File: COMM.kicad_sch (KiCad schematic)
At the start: 14 parts, among them J1 SMA Conn. (RFPC-SMA29-F), SW1 Inhibit Switch (SS5GLD2), U1 AX.25 Module (DMR818SU), U2 XBee Module (XBP9B-DMSTB002)

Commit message: Finished schematic and fully routed PCB.
Signed-off-by: Logan Tolbert <xem6df@virginia.edu>
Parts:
- removed J1: SMA Conn. (RFPC-SMA29-F), RFPC-SMA29-F:GRADCONN_RFPC-SMA29-F, symbol RFPC-SMA29-F:RFPC-SMA29-F
- removed U1: AX.25 Module (DMR818SU), DMR818S:DMR818SU, symbol DMR818S:DMR818S-U
- added D2: Voltage Converter DMR (1N4002), Diode_THT:D_DO-41_SOD81_P10.16mm_Horizontal, symbol Diode:1N4002
- added J1: SMA Conn. (RFPC-SMA30-F), RFPC-SMA30-F:GRADCONN_RFPC-SMA30-F, symbol RFPC-SMA30-F:RFPC-SMA30-F
- R2: value 10Ω -> 470 Ω
- renumbered D2 to D3, U2 to U1
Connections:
- net PWM0_XB is gone; now on net DIO10/PWM0_XB: U1.6 (DIO10/PWM0)
- net PWM1_XB is gone; now on net DIO11/PWM1_XB: U1.7 (DIO11/PWM1)
- net SLEEP_XB is gone; now on net ON_SLEEP/DIO9_XB: U1.13 (ON_NSLEEP/DIO9)
- net X_RESET is gone; now on net RESET_XB: U1.5 (~{RESET})
- net +3.3V: now also C2.1, C3.1, C4.1, U1.1 (VCC); no longer SW1.2 (B)
- net +5V: now also SW1.2 (B)
- net CS_DMR: now also H2.24; no longer H1.13
- net GND: now also J1.G1, J1.G2, J1.G3, J1.G4
- net HST_RXD_DMR: now also H2.25; no longer H1.19
- net HST_TXD_DMR: now also H2.27; no longer H1.17
- net PTT_DMR: now also H2.22; no longer H1.15
- net T/R_DMR: now also H2.21; no longer H1.11
- net UART_D_RX: no longer U1.3 (DIN/NCONFIG/DIO14)
- net UART_D_TX: no longer U1.2 (DOUT/DIO13)
- net DIO4/SPI_MOSI_XB: now reaches U1.11 (DIO4/SPI_MOSI)
- net DIO4/SPI_MOSI_XB: now also H2.7
- net Associate/DIO5_XB: now reaches D3.2 (A), U1.15 (ASSOCIATE/DIO5)
- net Associate/DIO5_XB: now also H2.16
- net AD3/DIO3/SPI_SSEL_XB: now reaches U1.17 (AD3/DIO3/SPI_NSSEL)
- net AD3/DIO3/SPI_SSEL_XB: now also H2.5
- net AD2/DIO2/SPI_CLK_XB: now reaches U1.18 (AD2/DIO2/SPI_CLK)
- net AD2/DIO2/SPI_CLK_XB: now also H2.6
- net AD1/DIO1/SPI_ATTN_XB: now reaches U1.19 (AD1/DIO1/SPI_NATTN)
- net AD1/DIO1/SPI_ATTN_XB: now also H2.10
- net DIO12/SPI_MISO: now reaches U1.4 (DIO12/SPI_MISO)
- net DIO12/SPI_MISO: now also H2.8
- net DTR/SLEEP_RQ/DIO8: now reaches U1.9 (NDTR/SLEEP_RQ/DIO8)
- net DTR/SLEEP_RQ/DIO8: now also H2.9
- net DIN/CONFIG/DIO14_XB: now reaches H2.1
- net DIN/CONFIG/DIO14_XB: now also U1.3 (DIN/NCONFIG/DIO14)
- net ON_SLEEP/DIO9_XB: now reaches H2.11
- net DIO10/PWM0_XB: now reaches H2.12
- net RESET_XB: now reaches H2.13
- net DIO11/PWM1_XB: now reaches H2.14
- net AD0/DIO0_XB: now reaches H2.15
- net AD0/DIO0_XB: now also U1.20 (AD0/DIO0)
- net NDTR_XB: now reaches H2.17
- net MIC_IN_DMR: now reaches H2.19
- net DOUT/DIO13_XB: now reaches H2.2
- net DOUT/DIO13_XB: now also U1.2 (DOUT/DIO13)
- net LINE_OUT_DMR: now reaches H2.20
- net SPKEN_DMR: now reaches H2.23
- net UART_RX_DMR: now reaches H2.26
- net UART_TX_DMR: now reaches H2.28
- net RTS/DOI6_XB: now reaches H2.3
- net RTS/DOI6_XB: now also U1.16 (NRTS/DIO6)
- net CTS/DIO7_XB: now reaches H2.4
- net CTS/DIO7_XB: now also U1.12 (NCTS/DIO7)
- net CTS_XB: no longer names the net of H1.5
- net CTS_XB: no longer U1.12 (NCTS/DIO7)
- net GPIO_XB: no longer names the net of H1.9
- net GPIO_XB: no longer U1.20 (AD0/DIO0)
- net RTS_XB: no longer names the net of H1.7
- net RTS_XB: no longer U1.16 (NRTS/DIO6)
- new net DMR818S-U 2W RF Module/ANT: J1.1
- new net DMR818S-U 2W RF Module/VCC: D2.1 (K)
- new net Voltage Converter XB/VIN: D2.2 (A), R2.2, SW1.1 (A)
- no-connect marks 0 -> 1
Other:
- sheet Voltage Converter renamed Voltage Converter XB
- added sheet DMR818S-U 2W RF Module (dmrRFMod.kicad_sch)
- moved on the sheet: C1, C2, C3, C4, D1, D3, H1, H2, R1, R2, SW1, U1

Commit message: Added 3D models to all components except DMR module, need to make a 3D model for that one.
Signed-off-by: Logan Tolbert <xem6df@virginia.edu>
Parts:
- R1: footprint Resistor_SMD:R_0805_2012Metric -> R_10kO:RESC1005X40N
- R2: footprint R_10OHM:RESC1005X40 -> R_470O:RESC6332X65N
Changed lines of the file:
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@@
 			)
 		)
-		(property "Footprint" "R_10OHM:RESC1005X40"
+		(property "Footprint" "R_470O:RESC6332X65N"
 			(at 127.254 63.246 90)
 			(effects
@@
 			)
 		)
-		(property "Footprint" "Resistor_SMD:R_0805_2012Metric"
+		(property "Footprint" "R_10kO:RESC1005X40N"
 			(at 115.824 48.006 90)
 			(effects

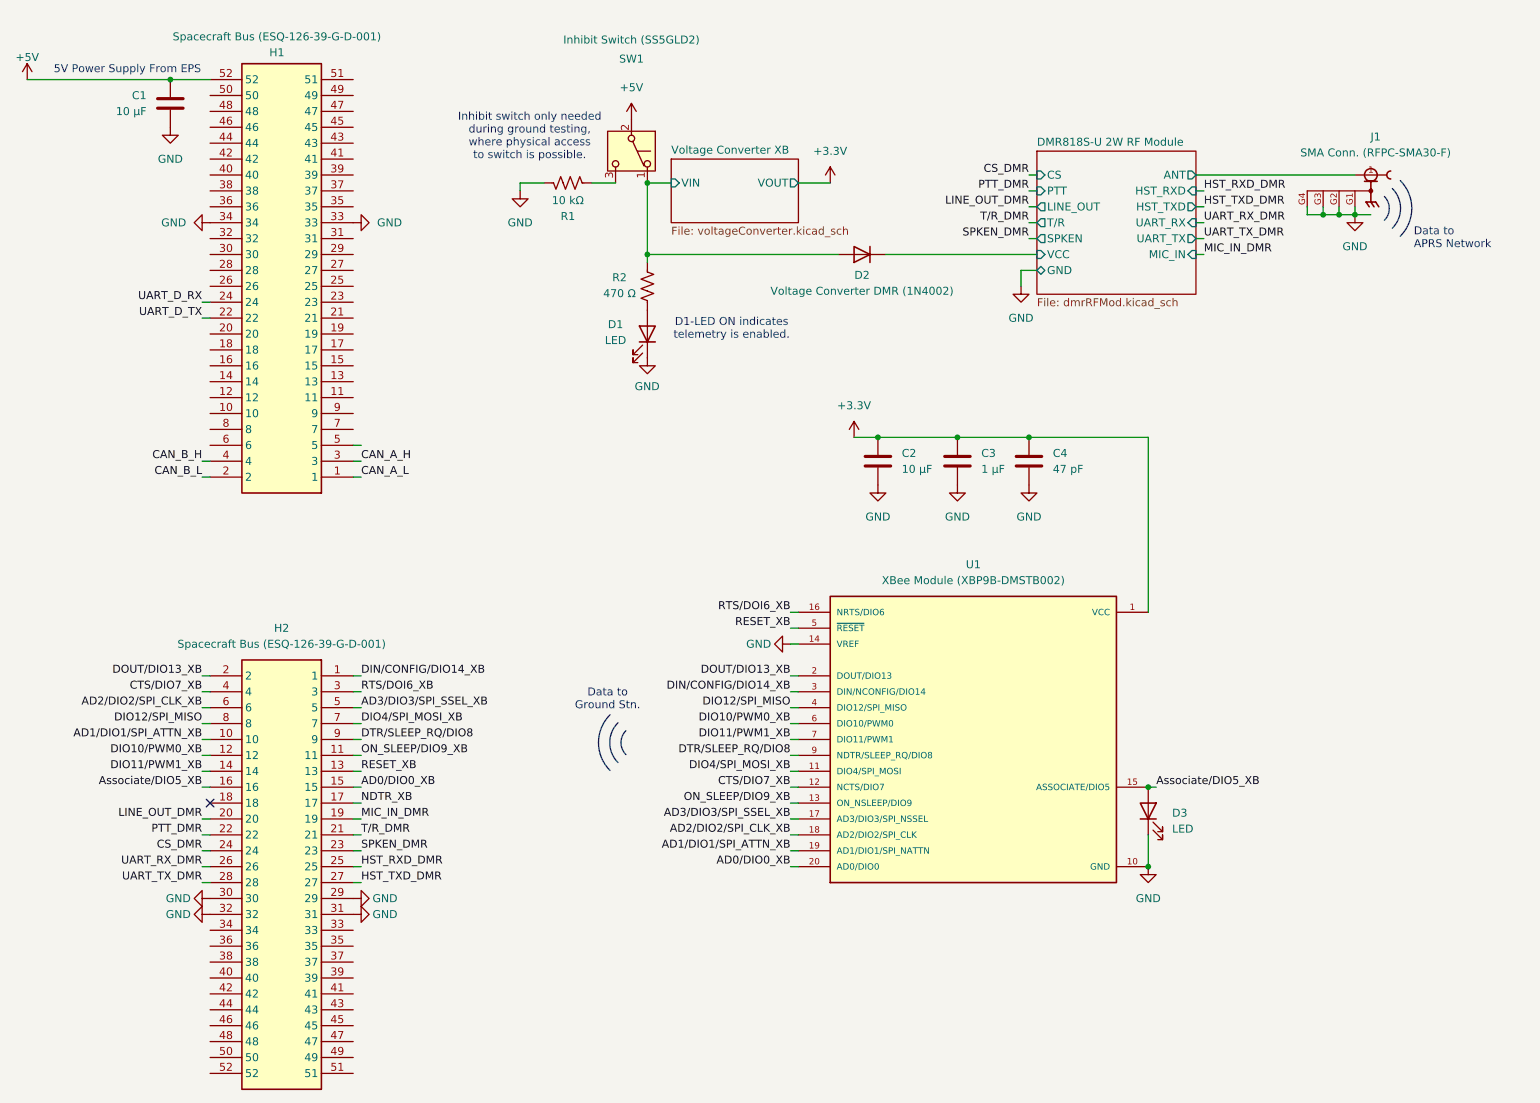
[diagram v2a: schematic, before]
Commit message: removed extraneous connections to the XBee and DMR modules on schematic and PCB.
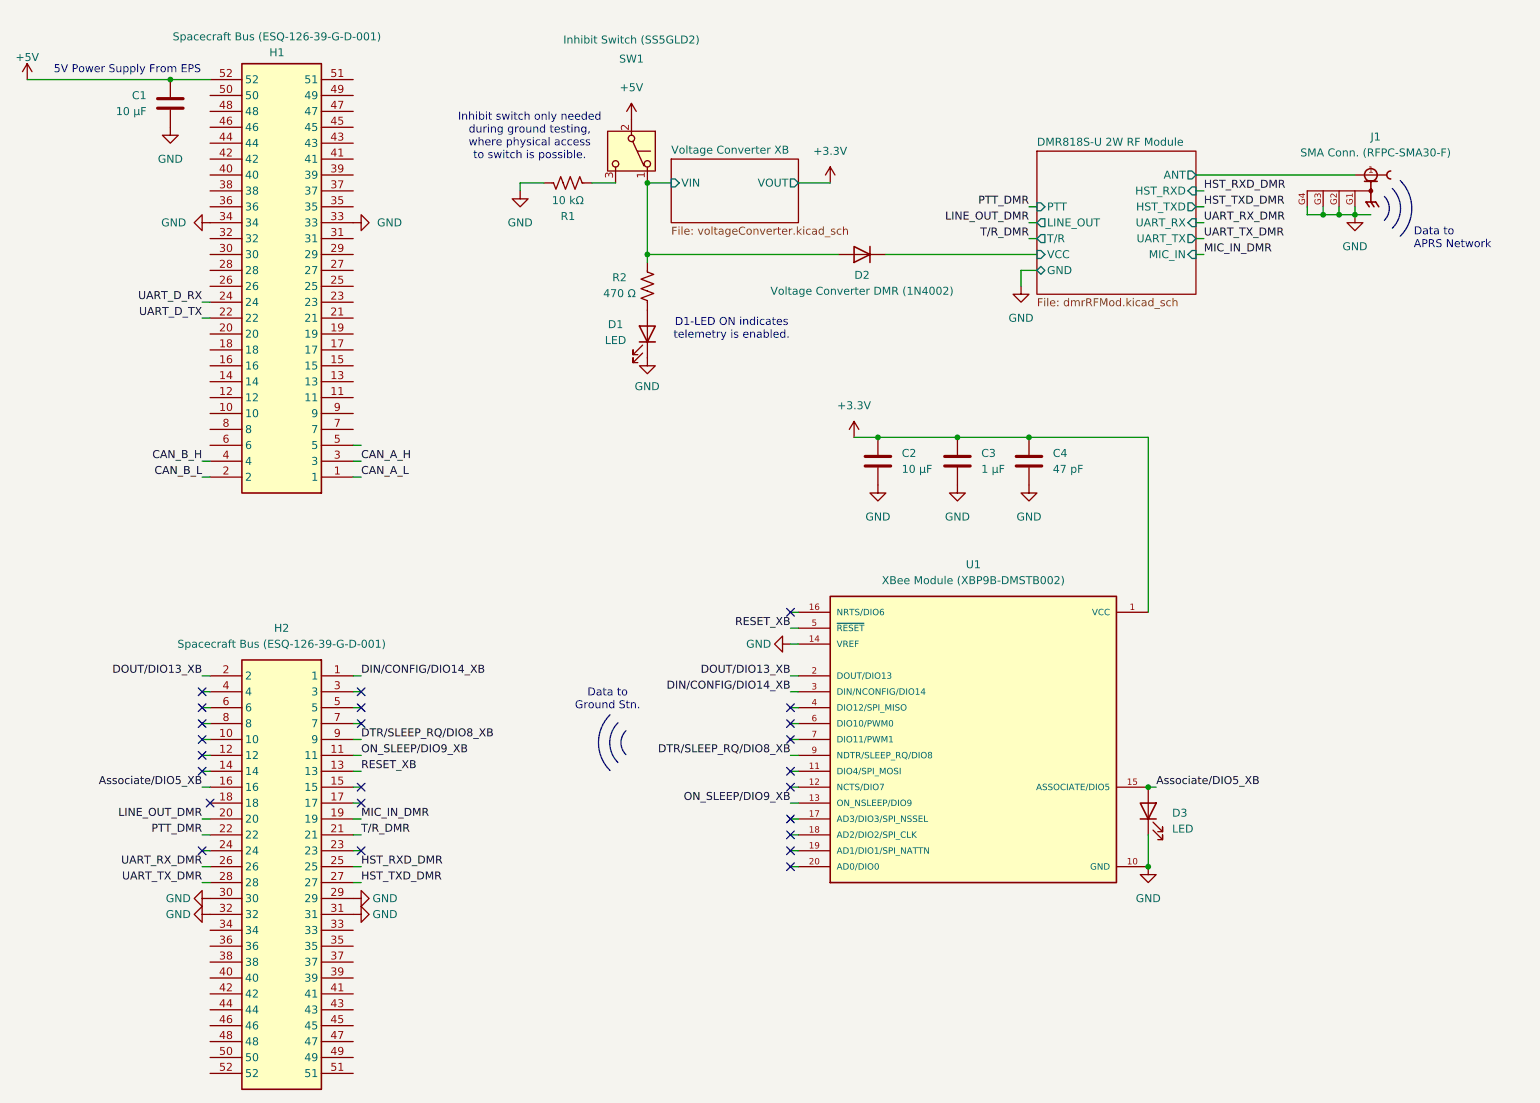
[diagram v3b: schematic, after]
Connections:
- net AD0/DIO0_XB: no longer names the net of U1.20 (AD0/DIO0)
- net AD0/DIO0_XB: no longer H2.15
- net AD1/DIO1/SPI_ATTN_XB: no longer names the net of U1.19 (AD1/DIO1/SPI_NATTN)
- net AD1/DIO1/SPI_ATTN_XB: no longer H2.10
- net AD2/DIO2/SPI_CLK_XB: no longer names the net of U1.18 (AD2/DIO2/SPI_CLK)
- net AD2/DIO2/SPI_CLK_XB: no longer H2.6
- net AD3/DIO3/SPI_SSEL_XB: no longer names the net of U1.17 (AD3/DIO3/SPI_NSSEL)
- net AD3/DIO3/SPI_SSEL_XB: no longer H2.5
- net CS_DMR: no longer names the net of H2.24
- net CTS/DIO7_XB: no longer names the net of U1.12 (NCTS/DIO7)
- net CTS/DIO7_XB: no longer H2.4
- net DIO10/PWM0_XB: no longer names the net of U1.6 (DIO10/PWM0)
- net DIO10/PWM0_XB: no longer H2.12
- net DIO11/PWM1_XB: no longer names the net of U1.7 (DIO11/PWM1)
- net DIO11/PWM1_XB: no longer H2.14
- net DIO12/SPI_MISO: no longer names the net of U1.4 (DIO12/SPI_MISO)
- net DIO12/SPI_MISO: no longer H2.8
- net DIO4/SPI_MOSI_XB: no longer names the net of U1.11 (DIO4/SPI_MOSI)
- net DIO4/SPI_MOSI_XB: no longer H2.7
- net DTR/SLEEP_RQ/DIO8 renamed DTR/SLEEP_RQ/DIO8_XB
- net NDTR_XB: no longer names the net of H2.17
- net RTS/DOI6_XB: no longer names the net of U1.16 (NRTS/DIO6)
- net RTS/DOI6_XB: no longer H2.3
- net SPKEN_DMR: no longer names the net of H2.23
- no-connect marks 1 -> 24
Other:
- sheet DMR818S-U 2W RF Module ports: added none; removed CS, SPKEN

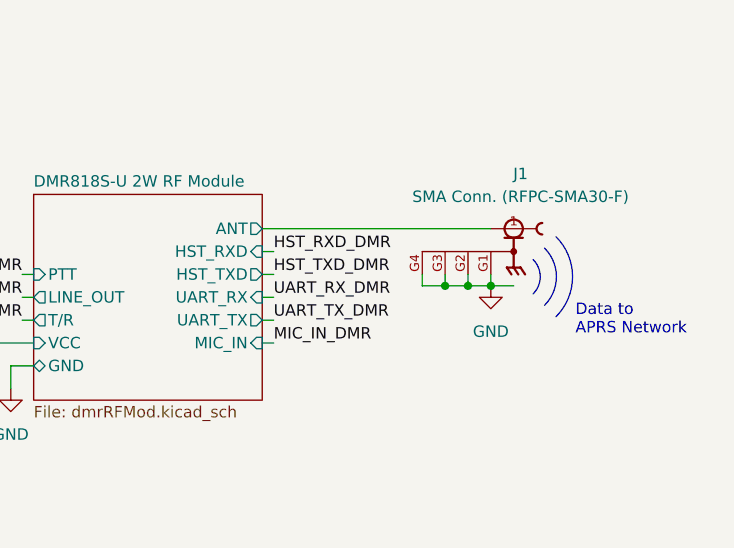
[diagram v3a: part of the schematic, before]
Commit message: Added pull-up to CS pin on DMR module.
Signed-off-by: Logan Tolbert <xem6df@virginia.edu>
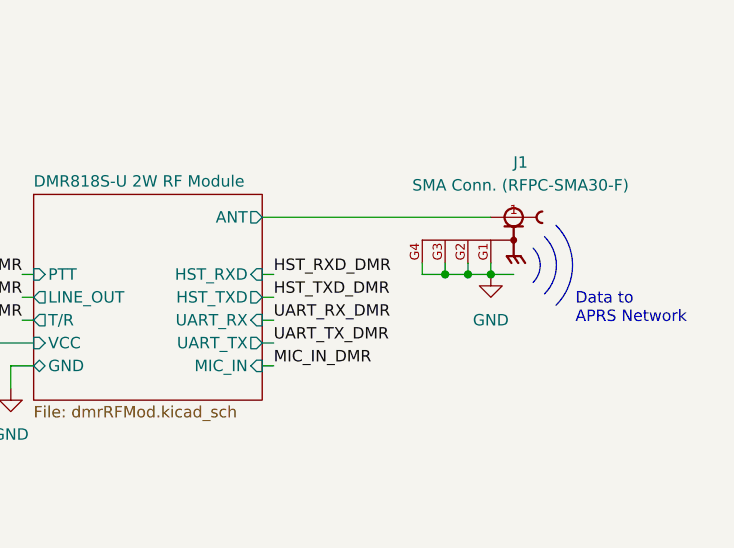
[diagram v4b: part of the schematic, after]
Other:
- moved on the sheet: J1
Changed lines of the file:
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@@
 	(paper "A4")
 	(arc
-		(start 248.5391 46.609)
-		(mid 250.3802 51.054)
-		(end 248.5391 55.499)
+		(start 248.5391 45.339)
+		(mid 250.3802 49.784)
+		(end 248.5391 54.229)
 		(stroke
 			(width 0)
@@
 	)
 	(arc
-		(start 247.2691 47.879)
-		(mid 248.586 51.054)
-		(end 247.2691 54.229)
+		(start 247.2691 46.609)
+		(mid 248.5831 49.7828)
+		(end 247.2691 52.959)
 		(stroke
 			(width 0)
@@
 	)
 	(arc
-		(start 245.9991 49.149)
-		(mid 246.7871 51.0528)
-		(end 245.9991 52.959)
+		(start 245.9991 47.879)
+		(mid 246.7842 49.7828)
+		(end 245.9991 51.689)
 		(stroke
 			(width 0)
@@
 	(text "Data to\nAPRS Network\n"
 		(exclude_from_sim no)
-		(at 250.698 55.88 0)
+		(at 250.698 54.61 0)
 		(effects
 			(font
@@
 	)
 	(junction
-		(at 238.76 52.07)
+		(at 238.76 50.8)
 		(diameter 0)
 		(color 0 0 0 0)
@@
 	)
 	(junction
-		(at 236.22 52.07)
+		(at 236.22 50.8)
 		(diameter 0)
 		(color 0 0 0 0)
@@
 	)
 	(junction
-		(at 241.3 52.07)
+		(at 241.3 50.8)
 		(diameter 0)
 		(color 0 0 0 0)
@@
 	(wire
 		(pts
-			(xy 215.9 45.72) (xy 241.3 45.72)
+			(xy 215.9 44.45) (xy 241.3 44.45)
 		)
 		(stroke
@@
 	(wire
 		(pts
-			(xy 241.3 52.07) (xy 238.76 52.07)
+			(xy 241.3 50.8) (xy 238.76 50.8)
 		)
 		(stroke
@@
 	(wire
 		(pts
-			(xy 217.17 53.34) (xy 215.9 53.34)
+			(xy 217.17 55.88) (xy 215.9 55.88)
 		)
 		(stroke
@@
 	(wire
 		(pts
-			(xy 238.76 50.8) (xy 238.76 52.07)
+			(xy 238.76 49.53) (xy 238.76 50.8)
 		)
 		(stroke
@@
 	(wire
 		(pts
-			(xy 241.3 52.07) (xy 241.3 50.8)
+			(xy 241.3 50.8) (xy 241.3 49.53)
 		)
 		(stroke
@@
 	(wire
 		(pts
-			(xy 236.22 50.8) (xy 236.22 52.07)
+			(xy 236.22 49.53) (xy 236.22 50.8)
 		)
 		(stroke
@@
 	(wire
 		(pts
-			(xy 236.22 52.07) (xy 233.68 52.07)
+			(xy 236.22 50.8) (xy 233.68 50.8)
 		)
 		(stroke
@@
 	(wire
 		(pts
-			(xy 217.17 50.8) (xy 215.9 50.8)
+			(xy 217.17 53.34) (xy 215.9 53.34)
 		)
 		(stroke
@@
 	(wire
 		(pts
-			(xy 241.3 52.07) (xy 243.84 52.07)
+			(xy 241.3 50.8) (xy 243.84 50.8)
 		)
 		(stroke
@@
 	(wire
 		(pts
-			(xy 217.17 58.42) (xy 215.9 58.42)
+			(xy 217.17 60.96) (xy 215.9 60.96)
 		)
 		(stroke
@@
 	(wire
 		(pts
-			(xy 236.22 52.07) (xy 238.76 52.07)
+			(xy 236.22 50.8) (xy 238.76 50.8)
 		)
 		(stroke
@@
 	(wire
 		(pts
-			(xy 217.17 48.26) (xy 215.9 48.26)
+			(xy 217.17 50.8) (xy 215.9 50.8)
 		)
 		(stroke
@@
 	(wire
 		(pts
-			(xy 217.17 55.88) (xy 215.9 55.88)
+			(xy 217.17 58.42) (xy 215.9 58.42)
 		)
 		(stroke
@@
 	(wire
 		(pts
-			(xy 233.68 52.07) (xy 233.68 50.8)
+			(xy 233.68 50.8) (xy 233.68 49.53)
 		)
 		(stroke
@@
 	)
 	(label "HST_RXD_DMR"
-		(at 217.17 48.26 0)
+		(at 217.17 50.8 0)
 		(effects
 			(font
@@
 	)
 	(label "MIC_IN_DMR"
-		(at 217.17 58.42 0)
+		(at 217.17 60.96 0)
 		(effects
 			(font
@@
 	)
 	(label "HST_TXD_DMR"
-		(at 217.17 50.8 0)
+		(at 217.17 53.34 0)
 		(effects
 			(font
@@
 	)
 	(label "UART_TX_DMR"
-		(at 217.17 55.88 0)
+		(at 217.17 58.42 0)
 		(effects
 			(font
@@
 	)
 	(label "UART_RX_DMR"
-		(at 217.17 53.34 0)
+		(at 217.17 55.88 0)
 		(effects
 			(font
@@
 		(dnp no)
 		(fields_autoplaced yes)
-		(property "Reference" "#PWR018"
+		(property "Reference" "#PWR017"
 			(at 187.96 69.85 0)
 			(effects
@@
 			(project "COMM"
 				(path "/b0bd204d-ca77-4624-acd2-31813bf00a6c"
-					(reference "#PWR018")
+					(reference "#PWR017")
 					(unit 1)
 				)
@@
 	(symbol
 		(lib_id "RFPC-SMA30-F:RFPC-SMA30-F")
-		(at 243.84 45.72 0)
+		(at 243.84 44.45 0)
 		(mirror y)
 		(unit 1)
@@
 		(dnp no)
 		(property "Reference" "J1"
-			(at 244.602 39.624 0)
+			(at 244.602 38.354 0)
 			(effects
 				(font
@@
 		)
 		(property "Value" "SMA Conn. (RFPC-SMA30-F)"
-			(at 244.602 42.164 0)
+			(at 244.602 40.894 0)
 			(effects
 				(font
@@
 		)
 		(property "Footprint" "RFPC-SMA30-F:GRADCONN_RFPC-SMA30-F"
-			(at 243.84 45.72 0)
+			(at 243.84 44.45 0)
 			(effects
 				(font
@@
 		)
 		(property "Datasheet" ""
-			(at 243.84 45.72 0)
+			(at 243.84 44.45 0)
 			(effects
 				(font
@@
 		)
 		(property "Description" ""
-			(at 243.84 45.72 0)
+			(at 243.84 44.45 0)
 			(effects
 				(font
@@
 		)
 		(property "PARTREV" "1.0"
-			(at 243.84 45.72 0)
+			(at 243.84 44.45 0)
 			(effects
 				(font
@@
 		)
 		(property "STANDARD" "Manufacturer Recommendations"
-			(at 243.84 45.72 0)
+			(at 243.84 44.45 0)
 			(effects
 				(font
@@
 		)
 		(property "MAXIMUM_PACKAGE_HEIGHT" "10.3mm"
-			(at 243.84 45.72 0)
+			(at 243.84 44.45 0)
 			(effects
 				(font
@@
 		)
 		(property "MANUFACTURER" "GradConn"
-			(at 243.84 45.72 0)
+			(at 243.84 44.45 0)
 			(effects
 				(font
@@
 		(on_board yes)
 		(dnp no)
-		(property "Reference" "#PWR017"
+		(property "Reference" "#PWR012"
 			(at 144.78 120.65 0)
 			(effects
@@
 			(project ""
 				(path "/b0bd204d-ca77-4624-acd2-31813bf00a6c"
-					(reference "#PWR017")
+					(reference "#PWR012")
 					(unit 1)
 				)
@@
 		(dnp no)
 		(fields_autoplaced yes)
-		(property "Reference" "#PWR020"
+		(property "Reference" "#PWR019"
 			(at 208.28 162.56 0)
 			(effects
@@
 			(project ""
 				(path "/b0bd204d-ca77-4624-acd2-31813bf00a6c"
-					(reference "#PWR020")
+					(reference "#PWR019")
 					(unit 1)
 				)
@@
 		(dnp no)
 		(fields_autoplaced yes)
-		(property "Reference" "#PWR012"
+		(property "Reference" "#PWR015"
 			(at 165.1 101.6 0)
 			(effects
@@
 			(project ""
 				(path "/b0bd204d-ca77-4624-acd2-31813bf00a6c"
-					(reference "#PWR012")
+					(reference "#PWR015")
 					(unit 1)
 				)
@@
 	(symbol
 		(lib_id "power:GND")
-		(at 241.3 52.07 0)
+		(at 241.3 50.8 0)
 		(mirror y)
 		(unit 1)
@@
 		(dnp no)
 		(fields_autoplaced yes)
-		(property "Reference" "#PWR019"
-			(at 241.3 58.42 0)
+		(property "Reference" "#PWR020"
+			(at 241.3 57.15 0)
 			(effects
 				(font
@@
 		)
 		(property "Value" "GND"
-			(at 241.3 57.15 0)
+			(at 241.3 55.88 0)
 			(effects
 				(font
@@
 		)
 		(property "Footprint" ""
-			(at 241.3 52.07 0)
+			(at 241.3 50.8 0)
 			(effects
 				(font
@@
 		)
 		(property "Datasheet" ""
-			(at 241.3 52.07 0)
+			(at 241.3 50.8 0)
 			(effects
 				(font
@@
 		)
 		(property "Description" "Power symbol creates a global label with name \"GND\" , ground"
-			(at 241.3 52.07 0)
+			(at 241.3 50.8 0)
 			(effects
 				(font
@@
 			(project ""
 				(path "/b0bd204d-ca77-4624-acd2-31813bf00a6c"
-					(reference "#PWR019")
+					(reference "#PWR020")
 					(unit 1)
 				)
@@
 		(dnp no)
 		(fields_autoplaced yes)
-		(property "Reference" "#PWR011"
+		(property "Reference" "#PWR014"
 			(at 161.29 91.44 0)
 			(effects
@@
 			(project "COMM"
 				(path "/b0bd204d-ca77-4624-acd2-31813bf00a6c"
-					(reference "#PWR011")
+					(reference "#PWR014")
 					(unit 1)
 				)
@@
 		(on_board yes)
 		(dnp no)
-		(property "Reference" "#PWR014"
+		(property "Reference" "#PWR011"
 			(at 128.27 81.28 0)
 			(effects
@@
 			(project "COMM"
 				(path "/b0bd204d-ca77-4624-acd2-31813bf00a6c"
-					(reference "#PWR014")
+					(reference "#PWR011")
 					(unit 1)
 				)
@@
 		(dnp no)
 		(fields_autoplaced yes)
-		(property "Reference" "#PWR016"
+		(property "Reference" "#PWR018"
 			(at 189.23 101.6 0)
 			(effects
@@
 			(project "COMM Board"
 				(path "/b0bd204d-ca77-4624-acd2-31813bf00a6c"
-					(reference "#PWR016")
+					(reference "#PWR018")
 					(unit 1)
 				)
@@
 		(dnp no)
 		(fields_autoplaced yes)
-		(property "Reference" "#PWR015"
+		(property "Reference" "#PWR016"
 			(at 177.8 101.6 0)
 			(effects
@@
 			(project "COMM Board"
 				(path "/b0bd204d-ca77-4624-acd2-31813bf00a6c"
-					(reference "#PWR015")
+					(reference "#PWR016")
 					(unit 1)
 				)
@@
 		)
 		(pin "ANT" output
-			(at 215.9 45.72 0)
+			(at 215.9 44.45 0)
 			(effects
 				(font
@@
 		)
 		(pin "HST_RXD" input
-			(at 215.9 48.26 0)
+			(at 215.9 50.8 0)
 			(effects
 				(font
@@
 		)
 		(pin "HST_TXD" output
-			(at 215.9 50.8 0)
+			(at 215.9 53.34 0)
 			(effects
 				(font
@@
 		)
 		(pin "MIC_IN" input
-			(at 215.9 58.42 0)
+			(at 215.9 60.96 0)
 			(effects
 				(font
@@
 		)
 		(pin "UART_RX" input
-			(at 215.9 53.34 0)
+			(at 215.9 55.88 0)
 			(effects
 				(font
@@
 		)
 		(pin "UART_TX" output
-			(at 215.9 55.88 0)
+			(at 215.9 58.42 0)
 			(effects
 				(font
